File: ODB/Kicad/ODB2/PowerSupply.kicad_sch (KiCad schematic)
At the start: 47 parts, among them J2 Batt3v7, J3 Batt12V, Q1 MMBT3904, Q2 IRFR5505TRPBF, Q3 PMOS, U2 TPS61201DRCR, U3 LM1085-5.0

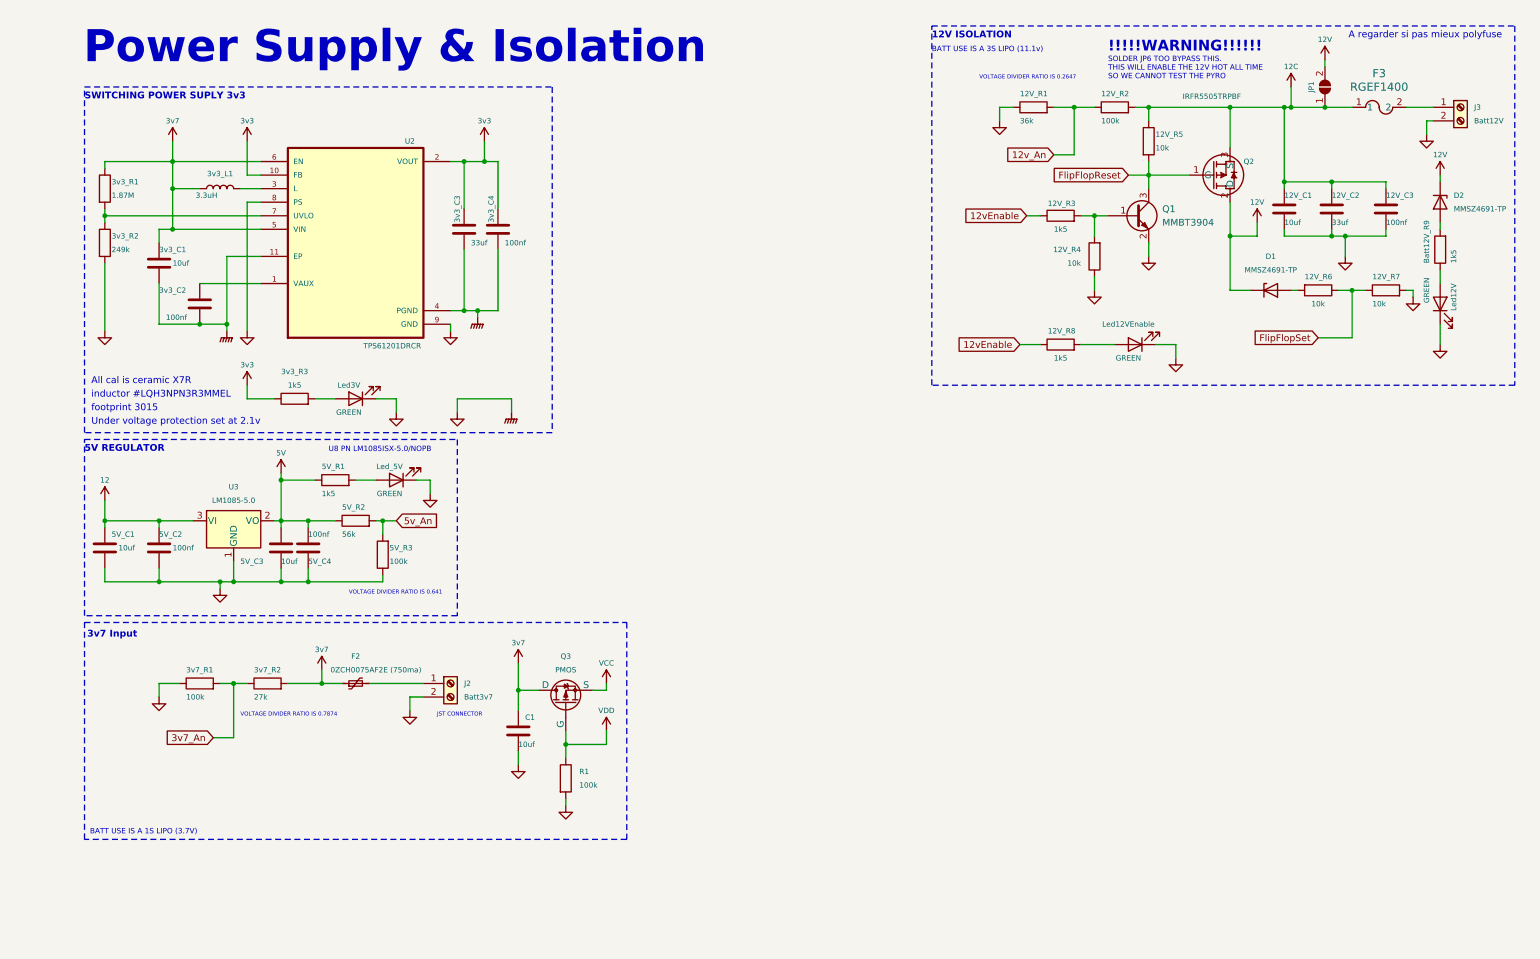
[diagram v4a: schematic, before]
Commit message: add SWDebug connector
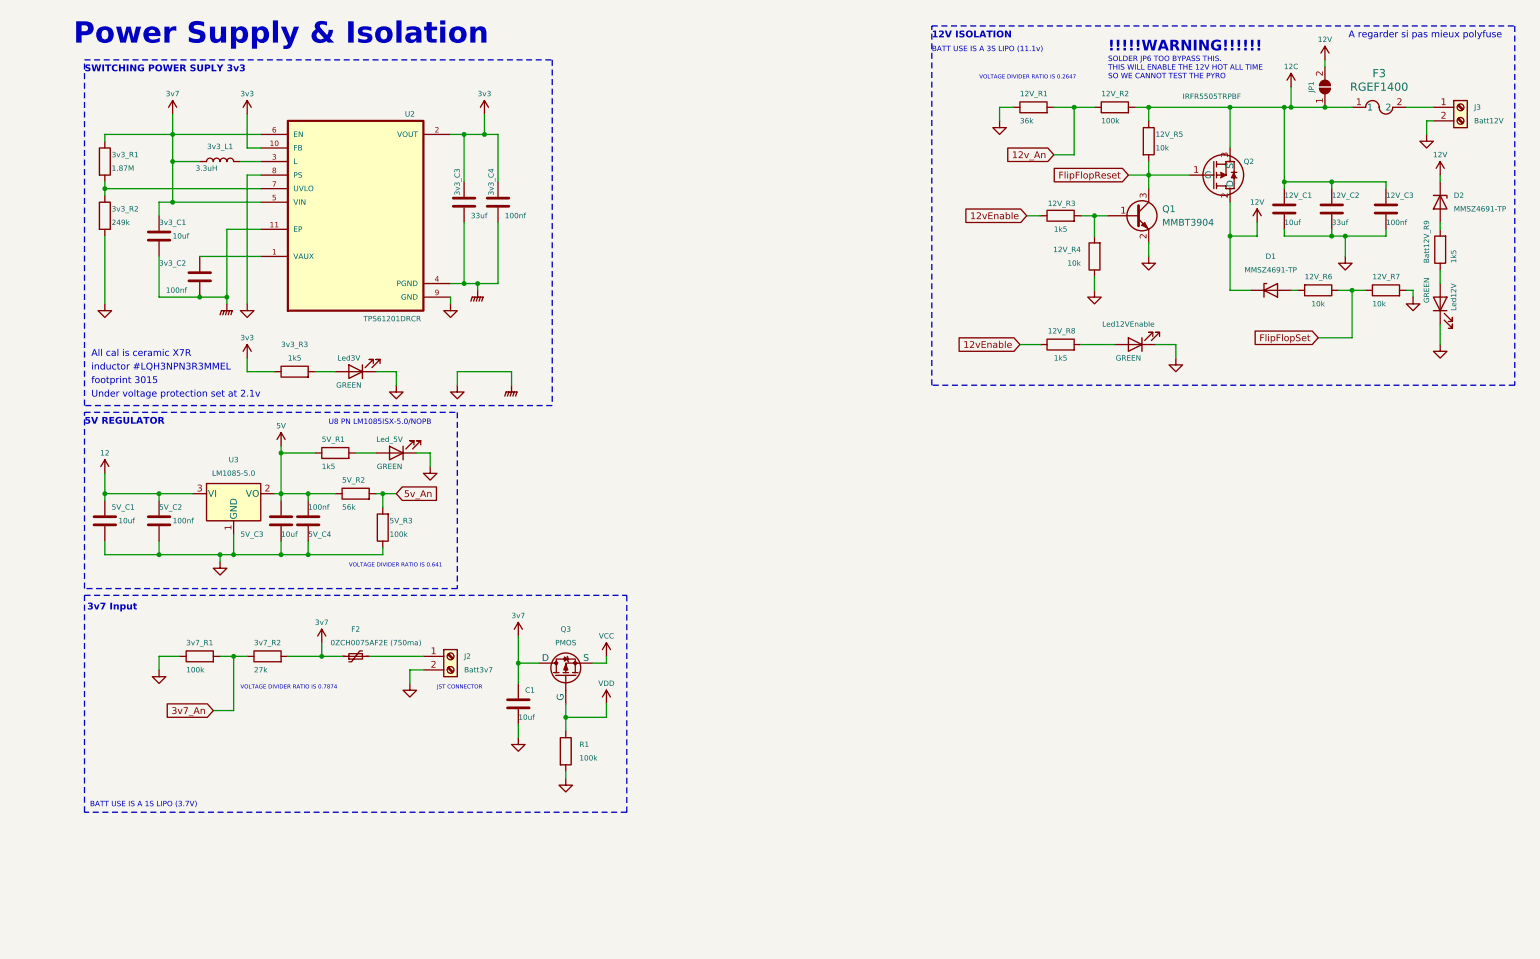
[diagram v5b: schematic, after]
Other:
- company: (none) -> GAUL
- title: (none) -> PowerSupply
- moved on the sheet: 3v3_C1, 3v3_C2, 3v3_C3, 3v3_C4, 3v3_L1, 3v3_R1, 3v3_R2, 3v3_R3, 3v7_R1, 3v7_R2, 5V_C1, 5V_C2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
